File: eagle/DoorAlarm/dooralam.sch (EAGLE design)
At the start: 2 parts

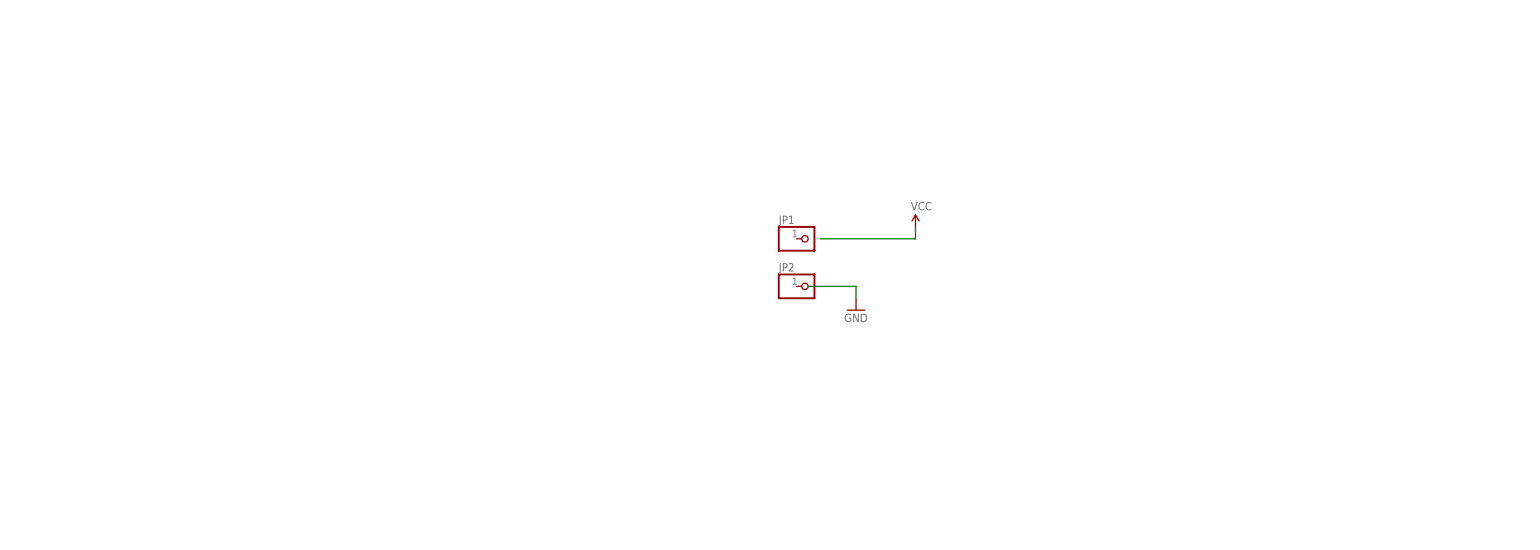
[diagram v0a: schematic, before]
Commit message: still need to add parts for low battery detection, but power supply is donw
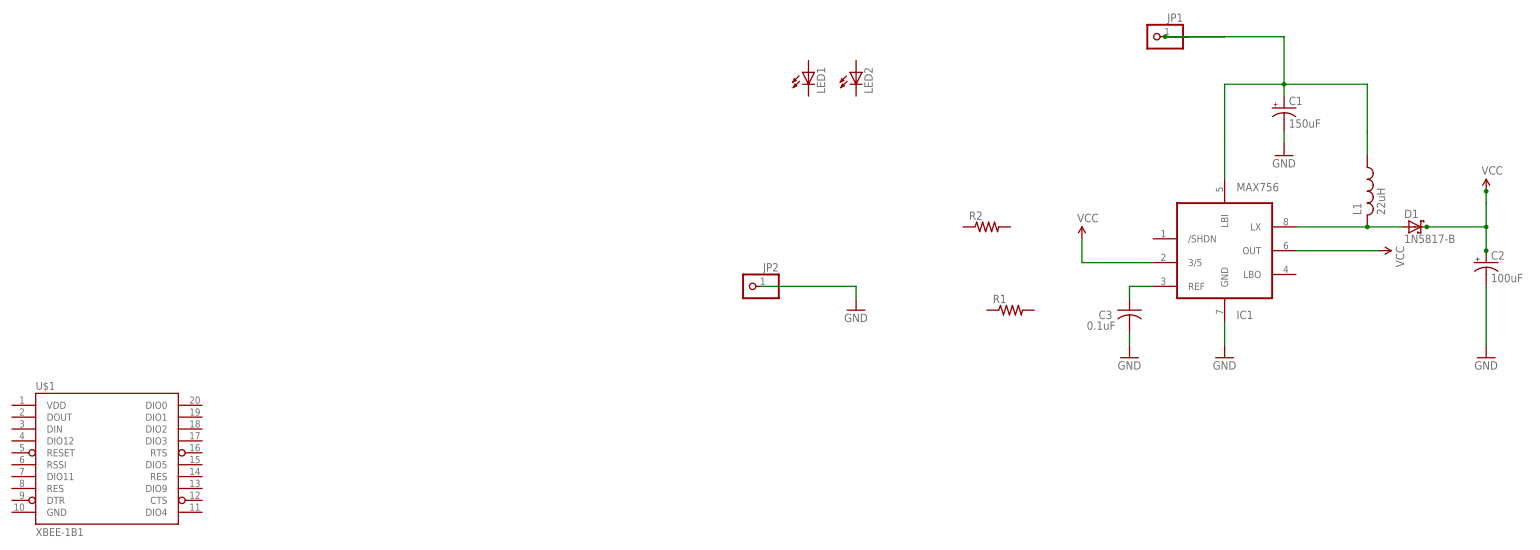
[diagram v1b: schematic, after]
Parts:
- added C1: 150uF, rcl:CPOL-USE2-5
- added C2: 100uF, rcl:CPOL-USE2-5
- added C3: 0.1uF, rcl:C-US025-025X050
- added D1: 1N5817-B, diode:1N5817-B
- added IC1: MAX756, usbbuck:MAX756CPA
- added L1: 22uH, usbbuck:L
- added LED1, LED2: (no value), led:LED3MM
- added R1, R2: (no value), rcl:R-US_0204/7
- added U$1: XBEE-1B1, SparkFun:XBEE-1B1
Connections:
- new net BATT+: C1.+, IC1.LBI, JP1.1, L1.1
- new net GND: C1.-, C2.-, C3.2, IC1.GND, JP2.1
- new net LX: D1.A, IC1.LX, L1.2
- new net N$1: C3.1, IC1.REF
- new net VCC: C2.+, D1.C, IC1.3/5, IC1.OUT
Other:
- moved on the sheet: JP1, JP2
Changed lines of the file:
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@@
 <part name="JP1" library="pinhead" deviceset="PINHD-1X1" device=""/>
 <part name="JP2" library="pinhead" deviceset="PINHD-1X1" device=""/>
-<part name="VCC" library="SparkFun" deviceset="VCC" device=""/>
+<part name="BATT+" library="SparkFun" deviceset="VCC" device=""/>
 <part name="GND1" library="SparkFun" deviceset="GND" device=""/>
+<part name="LED1" library="led" deviceset="LED" device="3MM"/>
+<part name="LED2" library="led" deviceset="LED" device="3MM"/>
+<part name="IC1" library="usbbuck" deviceset="MAX756" device="CPA" value="MAX756"/>
+<part name="U$1" library="SparkFun" deviceset="XBEE-1" device="B1"/>
+<part name="GND2" library="SparkFun" deviceset="GND" device=""/>
+<part name="L1" library="usbbuck" deviceset="L" device="" value="22uH"/>
+<part name="C1" library="rcl" deviceset="CPOL-US" device="E2-5" value="150uF"/>
+<part name="C2" library="rcl" deviceset="CPOL-US" device="E2-5" value="100uF"/>
+<part name="D1" library="diode" deviceset="1N581*" device="" technology="7-B"/>
+<part name="GND3" library="SparkFun" deviceset="GND" device=""/>
+<part name="GND4" library="SparkFun" deviceset="GND" device=""/>
+<part name="GND5" library="SparkFun" deviceset="GND" device=""/>
+<part name="BATT+1" library="SparkFun" deviceset="VCC" device=""/>
+<part name="BATT+2" library="SparkFun" deviceset="VCC" device=""/>
+<part name="C3" library="rcl" deviceset="C-US" device="025-025X050" value="0.1uF"/>
+<part name="R1" library="rcl" deviceset="R-US_" device="0204/7"/>
+<part name="R2" library="rcl" deviceset="R-US_" device="0204/7"/>
 </parts>
 <sheets>
@@
 </plain>
 <instances>
-<instance part="JP1" gate="G$1" x="15.24" y="76.2"/>
-<instance part="JP2" gate="G$1" x="15.24" y="66.04"/>
-<instance part="VCC" gate="1" x="38.1" y="78.74"/>
+<instance part="JP1" gate="G$1" x="88.9" y="119.38" rot="MR0"/>
+<instance part="JP2" gate="G$1" x="2.54" y="66.04" rot="MR0"/>
+<instance part="BATT+" gate="1" x="160.02" y="86.36"/>
 <instance part="GND1" gate="1" x="25.4" y="60.96"/>
+<instance part="LED1" gate="G$1" x="15.24" y="111.76"/>
+<instance part="LED2" gate="G$1" x="25.4" y="111.76"/>
+<instance part="IC1" gate="G$1" x="101.6" y="73.66" smashed="yes">
+<attribute name="NAME" x="106.68" y="59.055" size="1.778" layer="95"/>
+<attribute name="VALUE" x="106.68" y="86.36" size="1.778" layer="96"/>
+</instance>
+<instance part="U$1" gate="G$1" x="-134.62" y="30.48"/>
+<instance part="GND2" gate="1" x="104.14" y="50.8"/>
+<instance part="L1" gate="G$1" x="134.62" y="86.36"/>
+<instance part="C1" gate="G$1" x="116.84" y="104.14"/>
+<instance part="C2" gate="G$1" x="160.02" y="71.12" smashed="yes">
+<attribute name="NAME" x="161.036" y="71.755" size="1.778" layer="95"/>
+<attribute name="VALUE" x="161.036" y="66.929" size="1.778" layer="96"/>
+</instance>
+<instance part="D1" gate="G$1" x="144.78" y="78.74"/>
+<instance part="GND3" gate="1" x="160.02" y="50.8"/>
+<instance part="GND4" gate="1" x="83.82" y="50.8"/>
+<instance part="GND5" gate="1" x="116.84" y="93.98"/>
+<instance part="BATT+1" gate="1" x="73.66" y="76.2"/>
+<instance part="BATT+2" gate="1" x="137.16" y="73.66" rot="R270"/>
+<instance part="C3" gate="G$1" x="83.82" y="60.96" smashed="yes">
+<attribute name="NAME" x="77.216" y="59.055" size="1.778" layer="95"/>
+<attribute name="VALUE" x="74.676" y="56.769" size="1.778" layer="96"/>
+</instance>
+<instance part="R1" gate="G$1" x="58.42" y="60.96"/>
+<instance part="R2" gate="G$1" x="53.34" y="78.74"/>
 </instances>
 <busses>
@@
 <wire x1="15.24" y1="66.04" x2="25.4" y2="66.04" width="0.2032" layer="91"/>
 <wire x1="25.4" y1="66.04" x2="25.4" y2="63.5" width="0.2032" layer="91"/>
+<pinref part="JP2" gate="G$1" pin="1"/>
+<wire x1="5.08" y1="66.04" x2="15.24" y2="66.04" width="0.2032" layer="91"/>
+</segment>
+<segment>
+<pinref part="IC1" gate="G$1" pin="GND"/>
+<pinref part="GND2" gate="1" pin="GND"/>
+<wire x1="104.14" y1="58.42" x2="104.14" y2="53.34" width="0.2032" layer="91"/>
+</segment>
+<segment>
+<pinref part="C2" gate="G$1" pin="-"/>
+<pinref part="GND3" gate="1" pin="GND"/>
+<wire x1="160.02" y1="66.04" x2="160.02" y2="53.34" width="0.2032" layer="91"/>
+</segment>
+<segment>
+<pinref part="C1" gate="G$1" pin="-"/>
+<pinref part="GND5" gate="1" pin="GND"/>
+<wire x1="116.84" y1="99.06" x2="116.84" y2="96.52" width="0.1524" layer="91"/>
+</segment>
+<segment>
+<pinref part="C3" gate="G$1" pin="2"/>
+<pinref part="GND4" gate="1" pin="GND"/>
+<wire x1="83.82" y1="55.88" x2="83.82" y2="53.34" width="0.2032" layer="91"/>
+</segment>
+</net>
+<net name="BATT+" class="0">
+<segment>
+<wire x1="91.44" y1="119.38" x2="104.14" y2="119.38" width="0.2032" layer="91"/>
+<wire x1="96.52" y1="119.38" x2="91.44" y2="119.38" width="0.2032" layer="91"/>
+<wire x1="91.44" y1="119.38" x2="104.14" y2="119.38" width="0.2032" layer="91"/>
+<pinref part="JP1" gate="G$1" pin="1"/>
+<junction x="91.44" y="119.38"/>
+<wire x1="104.14" y1="119.38" x2="116.84" y2="119.38" width="0.2032" layer="91"/>
+<pinref part="IC1" gate="G$1" pin="LBI"/>
+<wire x1="104.14" y1="88.9" x2="104.14" y2="96.52" width="0.2032" layer="91"/>
+<wire x1="104.14" y1="96.52" x2="104.14" y2="109.22" width="0.2032" layer="91"/>
+<wire x1="104.14" y1="109.22" x2="116.84" y2="109.22" width="0.2032" layer="91"/>
+<pinref part="L1" gate="G$1" pin="1"/>
+<wire x1="116.84" y1="109.22" x2="134.62" y2="109.22" width="0.2032" layer="91"/>
+<wire x1="134.62" y1="99.06" x2="134.62" y2="93.98" width="0.2032" layer="91"/>
+<wire x1="134.62" y1="109.22" x2="134.62" y2="99.06" width="0.2032" layer="91"/>
+<wire x1="116.84" y1="119.38" x2="116.84" y2="109.22" width="0.2032" layer="91"/>
+<junction x="116.84" y="109.22"/>
+<pinref part="C1" gate="G$1" pin="+"/>
+<wire x1="116.84" y1="106.68" x2="116.84" y2="109.22" width="0.2032" layer="91"/>
+</segment>
+</net>
+<net name="LX" class="0">
+<segment>
+<pinref part="IC1" gate="G$1" pin="LX"/>
+<pinref part="L1" gate="G$1" pin="2"/>
+<wire x1="119.38" y1="78.74" x2="134.62" y2="78.74" width="0.2032" layer="91"/>
+<junction x="134.62" y="78.74"/>
+<pinref part="D1" gate="G$1" pin="A"/>
+<wire x1="142.24" y1="78.74" x2="134.62" y2="78.74" width="0.2032" layer="91"/>
 </segment>
 </net>
 <net name="VCC" class="0">
 <segment>
-<pinref part="VCC" gate="1" pin="VCC"/>
-<wire x1="17.78" y1="76.2" x2="38.1" y2="76.2" width="0.2032" layer="91"/>
-<wire x1="38.1" y1="76.2" x2="38.1" y2="78.74" width="0.2032" layer="91"/>
+<pinref part="D1" gate="G$1" pin="C"/>
+<wire x1="147.32" y1="78.74" x2="160.02" y2="78.74" width="0.2032" layer="91"/>
+<pinref part="C2" gate="G$1" pin="+"/>
+<wire x1="160.02" y1="78.74" x2="160.02" y2="73.66" width="0.2032" layer="91"/>
+<pinref part="BATT+" gate="1" pin="VCC"/>
+<wire x1="160.02" y1="86.36" x2="160.02" y2="83.82" width="0.2032" layer="91"/>
+<wire x1="160.02" y1="83.82" x2="160.02" y2="78.74" width="0.2032" layer="91"/>
+<junction x="160.02" y="78.74"/>
+<junction x="147.32" y="78.74"/>
+<junction x="160.02" y="73.66"/>
+<junction x="160.02" y="86.36"/>
+</segment>
+<segment>
+<pinref part="IC1" gate="G$1" pin="3/5"/>
+<wire x1="88.9" y1="71.12" x2="73.66" y2="71.12" width="0.2032" layer="91"/>
+<pinref part="BATT+1" gate="1" pin="VCC"/>
+<wire x1="73.66" y1="71.12" x2="73.66" y2="76.2" width="0.2032" layer="91"/>
+</segment>
+<segment>
+<pinref part="IC1" gate="G$1" pin="OUT"/>
+<pinref part="BATT+2" gate="1" pin="VCC"/>
+<wire x1="119.38" y1="73.66" x2="137.16" y2="73.66" width="0.2032" layer="91"/>
 </segment>
 </net>
+<net name="N$1" class="0">
+<segment>
+<pinref part="IC1" gate="G$1" pin="REF"/>
+<pinref part="C3" gate="G$1" pin="1"/>
+<wire x1="88.9" y1="66.04" x2="83.82" y2="66.04" width="0.2032" layer="91"/>
+<wire x1="83.82" y1="66.04" x2="83.82" y2="63.5" width="0.2032" layer="91"/>
+</segment>
+</net>
